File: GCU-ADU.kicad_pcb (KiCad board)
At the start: 2 copper layers, 48.6 x 32.4 mm, 5 parts, among them X1 SW_Push, Y1 SW_Push

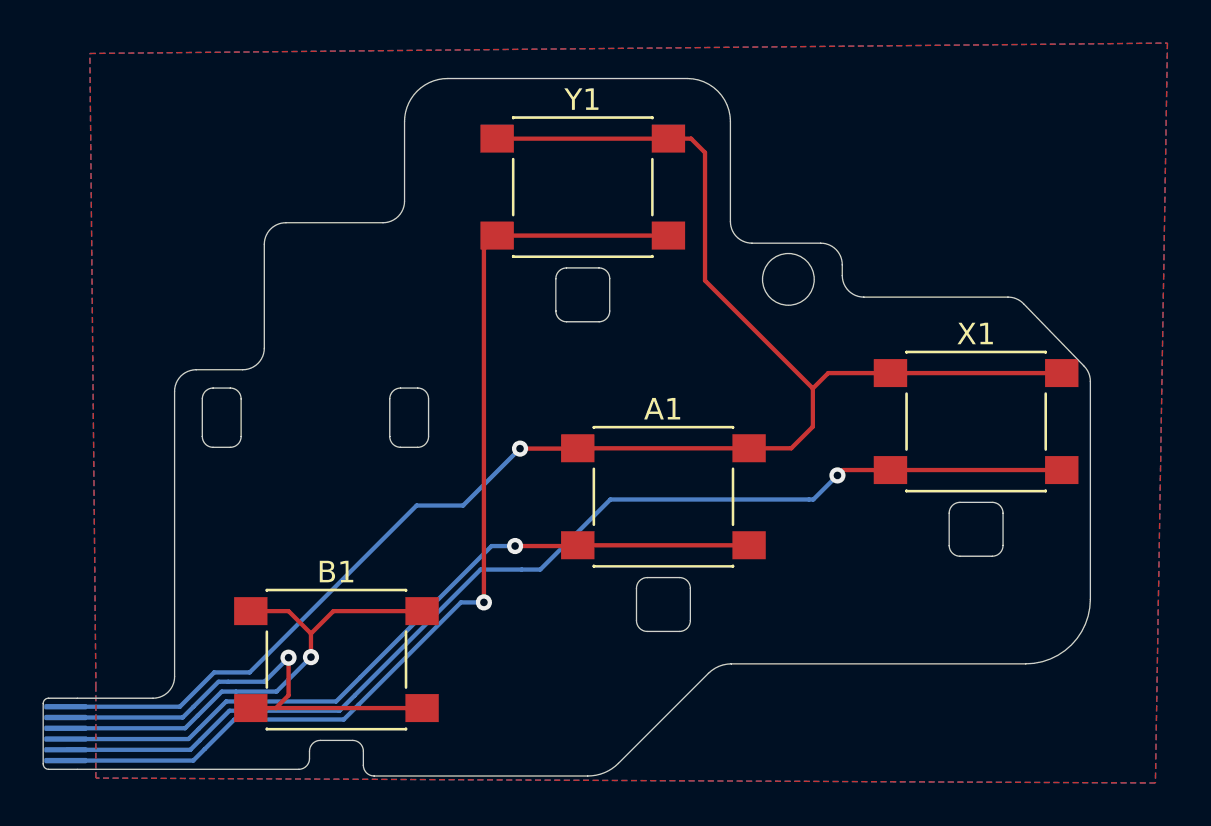
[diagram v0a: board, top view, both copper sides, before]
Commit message: Add switches to schematic
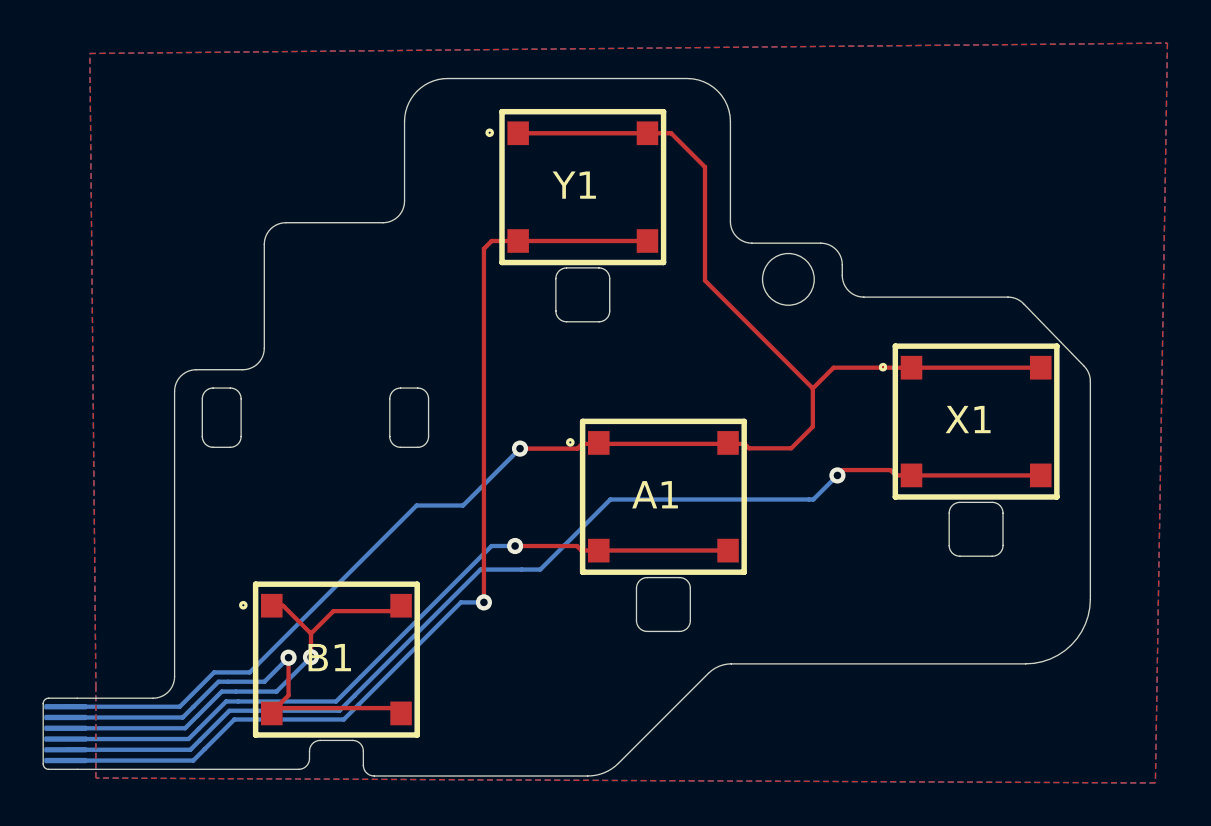
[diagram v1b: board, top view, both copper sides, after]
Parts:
- A1, B1, X1, Y1: footprint Button_Switch_SMD:SW_Push_1P1T_NO_6x6mm_H9.5mm -> hhl:SKRR
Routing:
- net X1: track 76.6 -> 74.7 mm
- net X6: track 22.7 -> 20.7 mm
- net X5: track 22.0 -> 20.2 mm
- net X4: track 47.7 -> 46.7 mm
- net X3: track 51.6 -> 50.7 mm
- net X2: track 35.4 -> 34.6 mm
